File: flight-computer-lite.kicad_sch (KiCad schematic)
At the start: 41 parts, among them J1 USB_C_Receptacle_USB2.0_16P, J2 Micro_SD_Card_Det2, J3 Conn_01x02_Pin, J4 Conn_01x03_Pin, Q1 BSS138, SW1 SW_Push, SW2 SW_Push, U1 RP2040, U2 W25Q32JVZP, Y1 SiT1602BI-22-33E-12.000000E

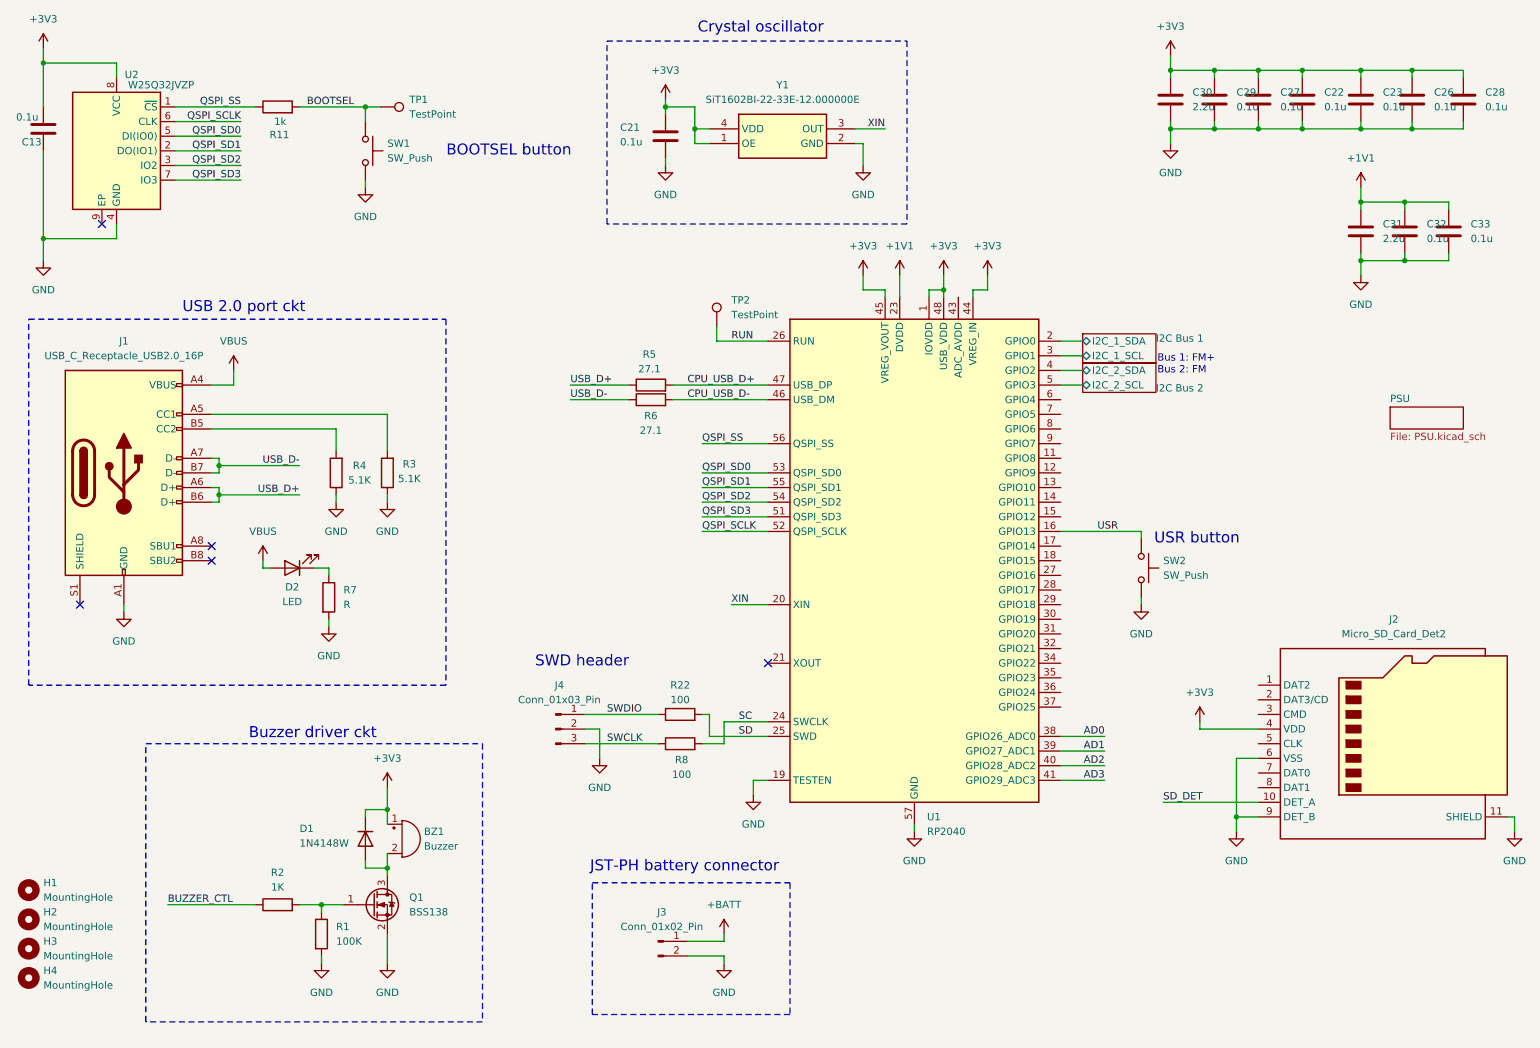
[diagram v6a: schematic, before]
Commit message: Tentatively finished schematic
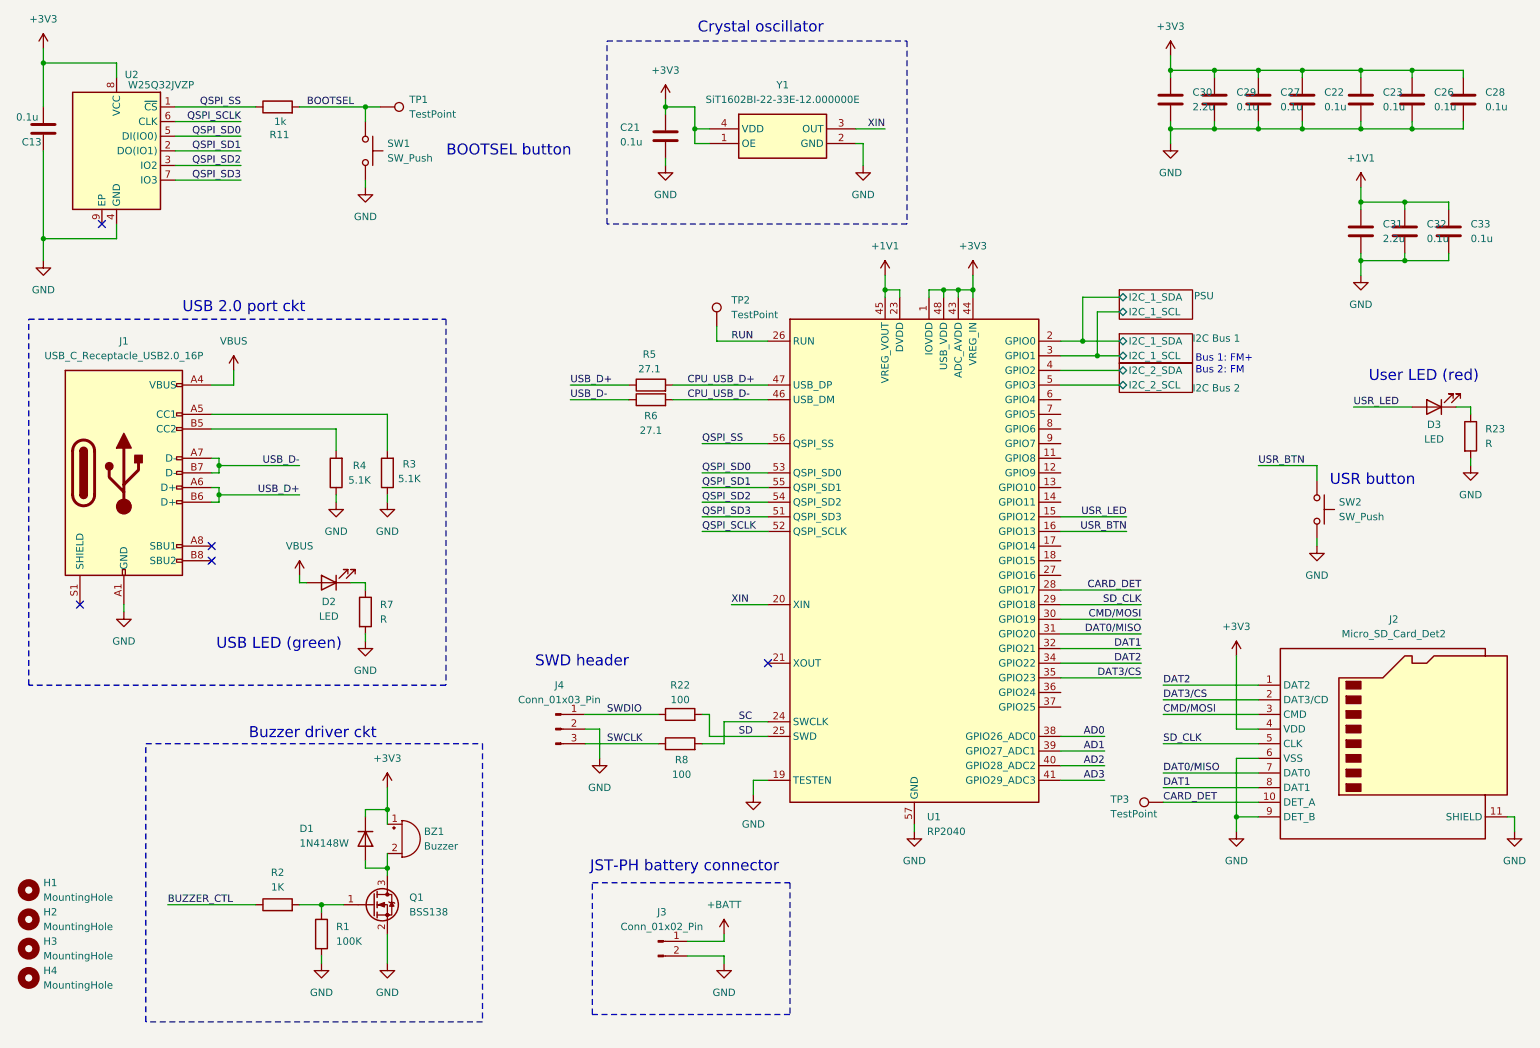
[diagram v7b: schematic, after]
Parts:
- added D3: LED, LED_SMD:LED_0603_1608Metric, symbol Device:LED
- added R23: R, Resistor_SMD:R_0603_1608Metric, symbol Device:R
- added TP3: TestPoint, TestPoint:TestPoint_Pad_D1.0mm, symbol Connector:TestPoint
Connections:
- net SD_DET is gone; now on net CARD_DET: J2.10 (DET_A)
- net +1V1: now also U1.45 (VREG_VOUT)
- net +3V3: now also U1.43 (ADC_AVDD); no longer U1.45 (VREG_VOUT)
- net GND: now also R23.2
- net USR_LED: now reaches U1.15 (GPIO12)
- net USR_LED: now also D3.2 (A)
- net CARD_DET: now reaches U1.28 (GPIO17)
- net CARD_DET: now also TP3.1
- net SD_CLK: now reaches U1.29 (GPIO18)
- net SD_CLK: now also J2.5 (CLK)
- net CMD/MOSI: now reaches U1.30 (GPIO19)
- net CMD/MOSI: now also J2.3 (CMD)
- net DAT0/MISO: now reaches U1.31 (GPIO20)
- net DAT0/MISO: now also J2.7 (DAT0)
- net DAT1: now reaches U1.32 (GPIO21)
- net DAT1: now also J2.8 (DAT1)
- net DAT2: now reaches U1.34 (GPIO22)
- net DAT2: now also J2.1 (DAT2)
- net DAT3/CS: now reaches U1.35 (GPIO23)
- net DAT3/CS: now also J2.2 (DAT3/CD)
- net USR renamed USR_BTN
- new net: D3.1 (K), R23.1
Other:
- sheet PSU ports: added I2C_1_SCL, I2C_1_SDA; removed none
- note added: "USB LED (green)"
- note added: "User LED (red)"
- moved on the sheet: D2, R7

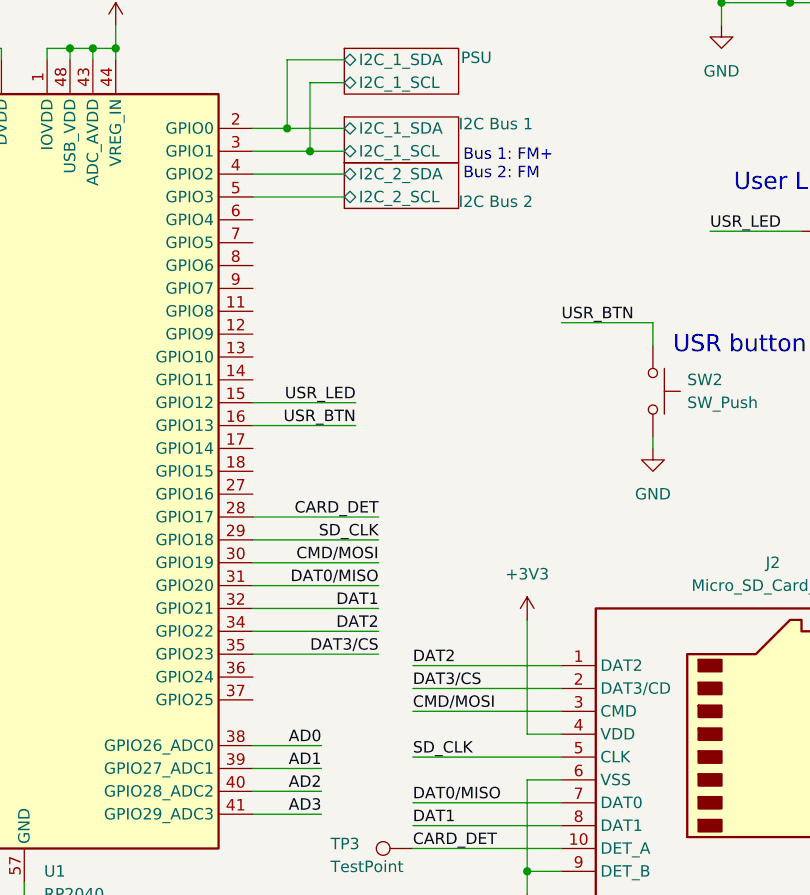
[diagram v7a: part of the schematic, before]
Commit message: Changed FM I2C bus pins
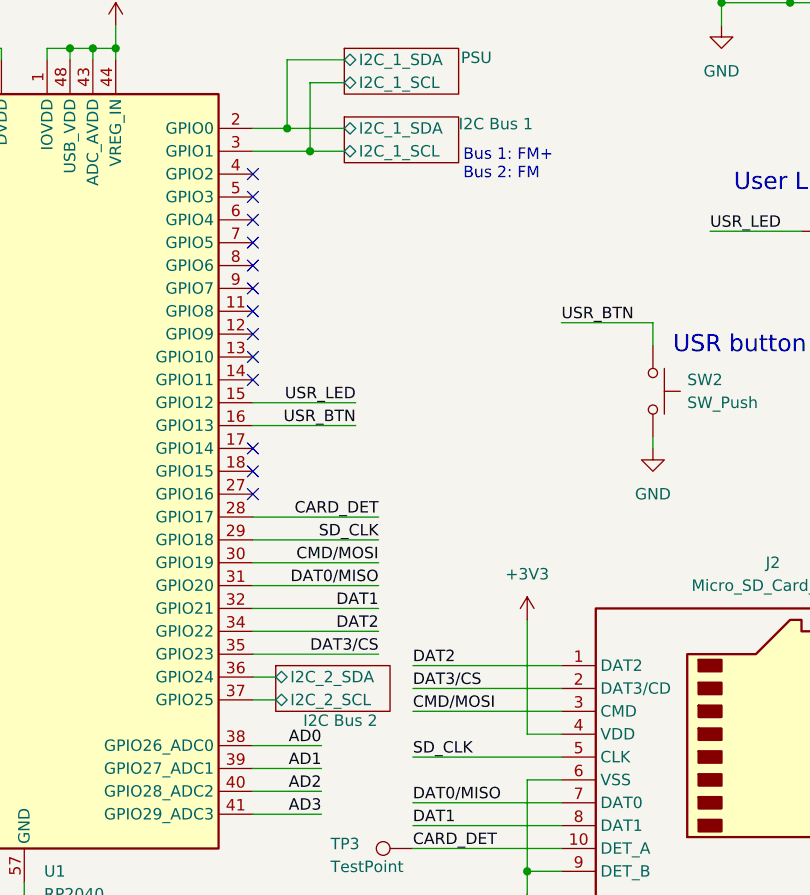
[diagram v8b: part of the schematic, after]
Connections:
- net I2C Bus 2/I2C_2_SCL: now also U1.37 (GPIO25); no longer U1.5 (GPIO3)
- net I2C Bus 2/I2C_2_SDA: now also U1.36 (GPIO24); no longer U1.4 (GPIO2)
- no-connect marks 5 -> 18
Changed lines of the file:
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@@
 	)
 	(no_connect
+		(at 199.39 113.03)
+	)
+	(no_connect
+		(at 199.39 87.63)
+	)
+	(no_connect
+		(at 199.39 95.25)
+	)
+	(no_connect
+		(at 199.39 92.71)
+	)
+	(no_connect
 		(at 52.07 107.95)
 	)
 	(no_connect
+		(at 199.39 77.47)
+	)
+	(no_connect
+		(at 199.39 97.79)
+	)
+	(no_connect
+		(at 199.39 82.55)
+	)
+	(no_connect
 		(at 148.59 128.27)
 	)
@@
 	)
 	(no_connect
+		(at 199.39 110.49)
+	)
+	(no_connect
 		(at 33.02 52.07)
 	)
+	(no_connect
+		(at 199.39 85.09)
+	)
+	(no_connect
+		(at 199.39 100.33)
+	)
+	(no_connect
+		(at 199.39 80.01)
+	)
+	(no_connect
+		(at 199.39 90.17)
+	)
+	(no_connect
+		(at 199.39 107.95)
+	)
 	(wire
 		(pts
@@
 	(wire
 		(pts
-			(xy 199.39 80.01) (xy 209.55 80.01)
-		)
-		(stroke
-			(width 0)
-			(type default)
-		)
-	)
-	(wire
-		(pts
 			(xy 53.34 99.06) (xy 53.34 100.33)
 		)
@@
 	(wire
 		(pts
+			(xy 199.39 135.89) (xy 201.93 135.89)
+		)
+		(stroke
+			(width 0)
+			(type default)
+		)
+	)
+	(wire
+		(pts
 			(xy 135.89 31.75) (xy 135.89 35.56)
 		)
@@
 	(wire
 		(pts
-			(xy 199.39 77.47) (xy 209.55 77.47)
-		)
-		(stroke
-			(width 0)
-			(type default)
-		)
-	)
-	(wire
-		(pts
 			(xy 269.24 35.56) (xy 269.24 34.29)
 		)
@@
 	(wire
 		(pts
+			(xy 199.39 133.35) (xy 201.93 133.35)
+		)
+		(stroke
+			(width 0)
+			(type default)
+		)
+	)
+	(wire
+		(pts
 			(xy 78.74 162.56) (xy 78.74 163.83)
 		)
@@
 	)
 	(sheet
-		(at 209.55 76.2)
+		(at 201.93 132.08)
 		(size 12.7 5.08)
 		(stroke
@@
 		)
 		(property "Sheetname" "I2C Bus 2"
-			(at 222.25 81.28 0)
+			(at 204.978 138.938 0)
 			(effects
 				(font
@@
 		)
 		(property "Sheetfile" "I2C_Bus_2.kicad_sch"
-			(at 209.55 80.5946 0)
+			(at 201.93 136.4746 0)
 			(effects
 				(font
@@
 		)
 		(pin "I2C_2_SCL" bidirectional
-			(at 209.55 80.01 180)
+			(at 201.93 135.89 180)
 			(effects
 				(font
@@
 		)
 		(pin "I2C_2_SDA" bidirectional
-			(at 209.55 77.47 180)
+			(at 201.93 133.35 180)
 			(effects
 				(font
